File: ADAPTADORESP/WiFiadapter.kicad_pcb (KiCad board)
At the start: 2 copper layers, 30 x 31.2 mm, 9 parts, among them J1 ADAP_ESP, U1 ESP8266-12E/ESP-12E

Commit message: PCBS_Adap_mon
Correxión del RX y TX del adaptador, PCB monitor doble capa.
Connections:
- J1 pad 7: /TX -> /RX
- J1 pad 9: /RX -> /TX
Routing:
- net /TX: track 48.8 -> 40.1 mm, vias 0 -> 1
- net GND: track 20.3 -> 16.3 mm
- net (no net): track 0.00 -> 3.97 mm
- net /RX: track 41.5 -> 45.3 mm
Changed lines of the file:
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@@
   (general
     (links 26)
-    (no_connects 0)
+    (no_connects 1)
     (area 134.899999 96.274999 165.075001 127.575001)
     (thickness 1.6)
     (drawings 6)
-    (tracks 198)
+    (tracks 200)
     (zones 0)
     (modules 9)
@@
       (net 7 /D3))
     (pad 7 thru_hole oval (at 0 7.62 90) (size 1.7 1.7) (drill 1) (layers *.Cu *.Mask)
-      (net 14 /TX))
+      (net 12 /RX))
     (pad 8 thru_hole oval (at 2.54 7.62 90) (size 1.7 1.7) (drill 1) (layers *.Cu *.Mask)
       (net 5 /D2))
     (pad 9 thru_hole oval (at 0 10.16 90) (size 1.7 1.7) (drill 1) (layers *.Cu *.Mask)
-      (net 12 /RX))
+      (net 14 /TX))
     (pad 10 thru_hole oval (at 2.54 10.16 90) (size 1.7 1.7) (drill 1) (layers *.Cu *.Mask)
       (net 10 /SDA))
@@
     (arrow2b (pts (xy 135.0264 83.7184) (xy 136.152904 83.131979)))
   )
+  (segment (start 139 121.95) (end 139 120.5) (width 0.5) (layer F.Cu) (net 0))
+  (segment (start 139 120.5) (end 138.4 119.9) (width 0.5) (layer F.Cu) (net 0))
+  (segment (start 140.2 123.1) (end 140.15 123.1) (width 0.5) (layer B.Cu) (net 0))
+  (segment (start 140.15 123.1) (end 139 121.95) (width 0.5) (layer B.Cu) (net 0))
   (segment (start 160.2 112.55) (end 159.05 112.55) (width 0.5) (layer F.Cu) (net 1))
   (segment (start 159.05 112.55) (end 158.85 112.35) (width 0.5) (layer F.Cu) (net 1))
@@
   (segment (start 157.1625 111.8281) (end 158.6625 111.8281) (width 0.5) (layer F.Cu) (net 1))
   (segment (start 158.6625 111.8281) (end 158.85 112.0156) (width 0.5) (layer F.Cu) (net 1))
-  (segment (start 139 121.95) (end 139 120.5) (width 0.5) (layer F.Cu) (net 1))
-  (segment (start 139 120.5) (end 138.4 119.9) (width 0.5) (layer F.Cu) (net 1))
-  (segment (start 140.2 123.1) (end 140.15 123.1) (width 0.5) (layer B.Cu) (net 1))
-  (segment (start 140.15 123.1) (end 139 121.95) (width 0.5) (layer B.Cu) (net 1))
   (segment (start 143.02 123.14) (end 140.24 123.14) (width 0.5) (layer F.Cu) (net 1))
   (segment (start 140.24 123.14) (end 140.2 123.1) (width 0.5) (layer F.Cu) (net 1))
@@
   (via (at 159.15 107.8) (size 1) (drill 0.4) (layers F.Cu B.Cu) (net 11))
   (segment (start 153.95 115.85) (end 158.2 115.85) (width 0.3) (layer B.Cu) (net 11))
-  (segment (start 153.75 125.2) (end 153.18 124.63) (width 0.3) (layer F.Cu) (net 12))
-  (segment (start 153.18 124.63) (end 153.18 123.14) (width 0.3) (layer F.Cu) (net 12))
-  (segment (start 163.35 100.925) (end 163.35 122.95) (width 0.3) (layer F.Cu) (net 12))
-  (segment (start 163.35 122.95) (end 161.1 125.2) (width 0.3) (layer F.Cu) (net 12))
-  (segment (start 161.1 125.2) (end 153.75 125.2) (width 0.3) (layer F.Cu) (net 12))
-  (segment (start 157.1625 99.8281) (end 162.2531 99.8281) (width 0.3) (layer F.Cu) (net 12))
-  (segment (start 162.2531 99.8281) (end 163.35 100.925) (width 0.3) (layer F.Cu) (net 12))
+  (segment (start 150.64 123.14) (end 150.64 124.615) (width 0.3) (layer F.Cu) (net 12) (status 400000))
+  (segment (start 162.3781 99.8281) (end 157.1625 99.8281) (width 0.3) (layer F.Cu) (net 12) (status 800000))
+  (segment (start 163.725 101.175) (end 162.3781 99.8281) (width 0.3) (layer F.Cu) (net 12))
+  (segment (start 163.725 123.45) (end 163.725 101.175) (width 0.3) (layer F.Cu) (net 12))
+  (segment (start 161.525 125.65) (end 163.725 123.45) (width 0.3) (layer F.Cu) (net 12))
+  (segment (start 151.675 125.65) (end 161.525 125.65) (width 0.3) (layer F.Cu) (net 12))
+  (segment (start 150.64 124.615) (end 151.675 125.65) (width 0.3) (layer F.Cu) (net 12))
   (segment (start 160.65 117.75) (end 160.65 122.4) (width 0.3) (layer B.Cu) (net 13))
   (segment (start 160.65 117) (end 160.65 117.75) (width 0.3) (layer B.Cu) (net 13))
@@
   (segment (start 159.1719 105.8281) (end 159.2 105.8) (width 0.3) (layer F.Cu) (net 13))
   (via (at 159.2 105.8) (size 1) (drill 0.4) (layers F.Cu B.Cu) (net 13))
-  (segment (start 150.64 125.24) (end 150.64 123.14) (width 0.3) (layer F.Cu) (net 14))
-  (segment (start 151.8 126.4) (end 150.64 125.24) (width 0.3) (layer F.Cu) (net 14))
-  (segment (start 157.1625 97.8281) (end 162.6281 97.8281) (width 0.3) (layer F.Cu) (net 14))
-  (segment (start 162.6281 97.8281) (end 164 99.2) (width 0.3) (layer F.Cu) (net 14))
-  (segment (start 164 99.2) (end 164 123.4) (width 0.3) (layer F.Cu) (net 14))
-  (segment (start 164 123.4) (end 161 126.4) (width 0.3) (layer F.Cu) (net 14))
-  (segment (start 161 126.4) (end 151.8 126.4) (width 0.3) (layer F.Cu) (net 14))
+  (segment (start 160.85 97.925) (end 157.2594 97.925) (width 0.3) (layer F.Cu) (net 14))
+  (segment (start 157.2594 97.925) (end 157.1625 97.8281) (width 0.3) (layer F.Cu) (net 14))
+  (segment (start 161.875 122.9) (end 161.875 98.95) (width 0.3) (layer B.Cu) (net 14))
+  (segment (start 161.875 98.95) (end 160.85 97.925) (width 0.3) (layer B.Cu) (net 14))
+  (via (at 160.85 97.925) (size 1) (drill 0.4) (layers F.Cu B.Cu) (net 14))
+  (segment (start 159.875 124.9) (end 161.875 122.9) (width 0.3) (layer B.Cu) (net 14))
+  (segment (start 153.737919 124.9) (end 159.875 124.9) (width 0.3) (layer B.Cu) (net 14))
+  (segment (start 153.18 123.14) (end 153.18 124.342081) (width 0.3) (layer B.Cu) (net 14))
+  (segment (start 153.18 124.342081) (end 153.737919 124.9) (width 0.3) (layer B.Cu) (net 14))
   (segment (start 139.35 101.8) (end 142.1344 101.8) (width 0.5) (layer F.Cu) (net 21))
   (segment (start 142.1344 101.8) (end 142.1625 101.8281) (width 0.5) (layer F.Cu) (net 21))

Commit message: Adapter_TXRX
TX RX change
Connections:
- J1 pad 7: /RX -> /TX
- J1 pad 9: /TX -> /RX
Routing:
- net /TX: track 40.1 -> 47.0 mm, vias 1 -> 0
- net /RX: track 45.3 -> 40.2 mm
- net (no net): track 3.97 -> 0.05 mm
- net /D0: track 34.8 -> 35.7 mm
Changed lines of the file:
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@@
-(kicad_pcb (version 4) (host pcbnew 4.0.6)
+(kicad_pcb (version 4) (host pcbnew 4.0.7)
   (general
     (links 26)
-    (no_connects 0)
+    (no_connects 2)
     (area 134.899999 96.274999 165.075001 127.575001)
     (thickness 1.6)
     (drawings 6)
-    (tracks 200)
+    (tracks 201)
     (zones 0)
     (modules 9)
@@
       (net 7 /D3))
     (pad 7 thru_hole oval (at 0 7.62 90) (size 1.7 1.7) (drill 1) (layers *.Cu *.Mask)
-      (net 12 /RX))
+      (net 14 /TX))
     (pad 8 thru_hole oval (at 2.54 7.62 90) (size 1.7 1.7) (drill 1) (layers *.Cu *.Mask)
       (net 5 /D2))
     (pad 9 thru_hole oval (at 0 10.16 90) (size 1.7 1.7) (drill 1) (layers *.Cu *.Mask)
-      (net 14 /TX))
+      (net 12 /RX))
     (pad 10 thru_hole oval (at 2.54 10.16 90) (size 1.7 1.7) (drill 1) (layers *.Cu *.Mask)
       (net 10 /SDA))
@@
     (arrow2b (pts (xy 135.0264 83.7184) (xy 136.152904 83.131979)))
   )
-  (segment (start 139 121.95) (end 139 120.5) (width 0.5) (layer F.Cu) (net 0))
-  (segment (start 139 120.5) (end 138.4 119.9) (width 0.5) (layer F.Cu) (net 0))
   (segment (start 140.2 123.1) (end 140.15 123.1) (width 0.5) (layer B.Cu) (net 0))
-  (segment (start 140.15 123.1) (end 139 121.95) (width 0.5) (layer B.Cu) (net 0))
+  (segment (start 143.02 123.14) (end 140.24 123.14) (width 0.5) (layer F.Cu) (net 1))
   (segment (start 160.2 112.55) (end 159.05 112.55) (width 0.5) (layer F.Cu) (net 1))
   (segment (start 159.05 112.55) (end 158.85 112.35) (width 0.5) (layer F.Cu) (net 1))
@@
   (segment (start 157.1625 111.8281) (end 158.6625 111.8281) (width 0.5) (layer F.Cu) (net 1))
   (segment (start 158.6625 111.8281) (end 158.85 112.0156) (width 0.5) (layer F.Cu) (net 1))
-  (segment (start 143.02 123.14) (end 140.24 123.14) (width 0.5) (layer F.Cu) (net 1))
   (segment (start 140.24 123.14) (end 140.2 123.1) (width 0.5) (layer F.Cu) (net 1))
   (via (at 156.875 114.4) (size 1.2) (drill 0.6) (layers F.Cu B.Cu) (net 1))
@@
   (segment (start 139.9 107) (end 140.3 106.6) (width 0.3) (layer F.Cu) (net 3))
   (segment (start 140.3 106.6) (end 140.3 106.15) (width 0.3) (layer F.Cu) (net 3))
+  (segment (start 145.56 124.342081) (end 144.66 125.242081) (width 0.3) (layer F.Cu) (net 4))
+  (segment (start 140 125.375) (end 144.527081 125.375) (width 0.3) (layer F.Cu) (net 4))
+  (segment (start 144.527081 125.375) (end 144.66 125.242081) (width 0.3) (layer F.Cu) (net 4))
   (segment (start 137.075 122.5) (end 137.075 106.95) (width 0.3) (layer F.Cu) (net 4))
   (segment (start 137.075 106.95) (end 137.625 106.4) (width 0.3) (layer F.Cu) (net 4))
@@
   (segment (start 139.75 105.8) (end 139.75 104.5281) (width 0.3) (layer F.Cu) (net 4))
   (segment (start 140.45 103.8281) (end 142.1625 103.8281) (width 0.3) (layer F.Cu) (net 4))
-  (segment (start 141.7 125.4) (end 140.925 125.4) (width 0.3) (layer F.Cu) (net 4))
   (segment (start 140 125.375) (end 141.675 125.375) (width 0.3) (layer F.Cu) (net 4))
   (segment (start 145.56 123.14) (end 145.56 124.342081) (width 0.3) (layer F.Cu) (net 4))
-  (segment (start 144.502081 125.4) (end 141.7 125.4) (width 0.3) (layer F.Cu) (net 4))
   (segment (start 141.675 125.375) (end 141.7 125.4) (width 0.3) (layer F.Cu) (net 4))
-  (segment (start 145.56 124.342081) (end 144.502081 125.4) (width 0.3) (layer F.Cu) (net 4))
   (segment (start 140 125.375) (end 137.075 122.45) (width 0.3) (layer F.Cu) (net 4))
   (segment (start 150.64 120.6) (end 150.64 116.79) (width 0.3) (layer F.Cu) (net 5))
@@
   (via (at 159.15 107.8) (size 1) (drill 0.4) (layers F.Cu B.Cu) (net 11))
   (segment (start 153.95 115.85) (end 158.2 115.85) (width 0.3) (layer B.Cu) (net 11))
-  (segment (start 150.64 123.14) (end 150.64 124.615) (width 0.3) (layer F.Cu) (net 12))
-  (segment (start 162.3781 99.8281) (end 157.1625 99.8281) (width 0.3) (layer F.Cu) (net 12))
-  (segment (start 163.725 101.175) (end 162.3781 99.8281) (width 0.3) (layer F.Cu) (net 12))
-  (segment (start 163.725 123.45) (end 163.725 101.175) (width 0.3) (layer F.Cu) (net 12))
-  (segment (start 161.525 125.65) (end 163.725 123.45) (width 0.3) (layer F.Cu) (net 12))
-  (segment (start 151.675 125.65) (end 161.525 125.65) (width 0.3) (layer F.Cu) (net 12))
-  (segment (start 150.64 124.615) (end 151.675 125.65) (width 0.3) (layer F.Cu) (net 12))
+  (segment (start 153.18 123.14) (end 153.18 124.45) (width 0.3) (layer F.Cu) (net 12))
+  (segment (start 153.18 124.45) (end 153.48 124.75) (width 0.3) (layer F.Cu) (net 12))
+  (segment (start 158.4625 99.8281) (end 157.1625 99.8281) (width 0.3) (layer F.Cu) (net 12))
+  (segment (start 153.48 124.75) (end 159.64 124.75) (width 0.3) (layer F.Cu) (net 12))
+  (segment (start 159.64 124.75) (end 163.54 120.85) (width 0.3) (layer F.Cu) (net 12))
+  (segment (start 163.54 120.85) (end 163.54 100.91) (width 0.3) (layer F.Cu) (net 12))
+  (segment (start 163.54 100.91) (end 162.46 99.83) (width 0.3) (layer F.Cu) (net 12))
+  (segment (start 162.46 99.83) (end 158.4644 99.83) (width 0.3) (layer F.Cu) (net 12))
+  (segment (start 158.4644 99.83) (end 158.4625 99.8281) (width 0.3) (layer F.Cu) (net 12))
   (segment (start 160.65 117.75) (end 160.65 122.4) (width 0.3) (layer B.Cu) (net 13))
   (segment (start 160.65 117) (end 160.65 117.75) (width 0.3) (layer B.Cu) (net 13))
@@
   (segment (start 159.1719 105.8281) (end 159.2 105.8) (width 0.3) (layer F.Cu) (net 13))
   (via (at 159.2 105.8) (size 1) (drill 0.4) (layers F.Cu B.Cu) (net 13))
-  (segment (start 160.85 97.925) (end 157.2594 97.925) (width 0.3) (layer F.Cu) (net 14))
+  (segment (start 150.63 124.6) (end 150.64 124.59) (width 0.3) (layer F.Cu) (net 14))
+  (segment (start 150.64 124.59) (end 150.64 123.14) (width 0.3) (layer F.Cu) (net 14))
+  (segment (start 151.460008 125.430008) (end 150.63 124.6) (width 0.3) (layer F.Cu) (net 14))
+  (segment (start 164.38 121.2) (end 160.149992 125.430008) (width 0.3) (layer F.Cu) (net 14))
+  (segment (start 160.149992 125.430008) (end 151.460008 125.430008) (width 0.3) (layer F.Cu) (net 14))
+  (segment (start 164.38 99.72) (end 164.38 121.2) (width 0.3) (layer F.Cu) (net 14))
+  (segment (start 162.585 97.925) (end 164.38 99.72) (width 0.3) (layer F.Cu) (net 14))
+  (segment (start 160.67 97.925) (end 157.2594 97.925) (width 0.3) (layer F.Cu) (net 14))
+  (segment (start 160.85 97.925) (end 160.67 97.925) (width 0.3) (layer F.Cu) (net 14))
+  (segment (start 160.67 97.925) (end 162.585 97.925) (width 0.3) (layer F.Cu) (net 14))
   (segment (start 157.2594 97.925) (end 157.1625 97.8281) (width 0.3) (layer F.Cu) (net 14))
-  (segment (start 161.875 122.9) (end 161.875 98.95) (width 0.3) (layer B.Cu) (net 14))
-  (segment (start 161.875 98.95) (end 160.85 97.925) (width 0.3) (layer B.Cu) (net 14))
-  (via (at 160.85 97.925) (size 1) (drill 0.4) (layers F.Cu B.Cu) (net 14))
-  (segment (start 159.875 124.9) (end 161.875 122.9) (width 0.3) (layer B.Cu) (net 14))
-  (segment (start 153.737919 124.9) (end 159.875 124.9) (width 0.3) (layer B.Cu) (net 14))
-  (segment (start 153.18 123.14) (end 153.18 124.342081) (width 0.3) (layer B.Cu) (net 14))
-  (segment (start 153.18 124.342081) (end 153.737919 124.9) (width 0.3) (layer B.Cu) (net 14))
   (segment (start 139.35 101.8) (end 142.1344 101.8) (width 0.5) (layer F.Cu) (net 21))
   (segment (start 142.1344 101.8) (end 142.1625 101.8281) (width 0.5) (layer F.Cu) (net 21))

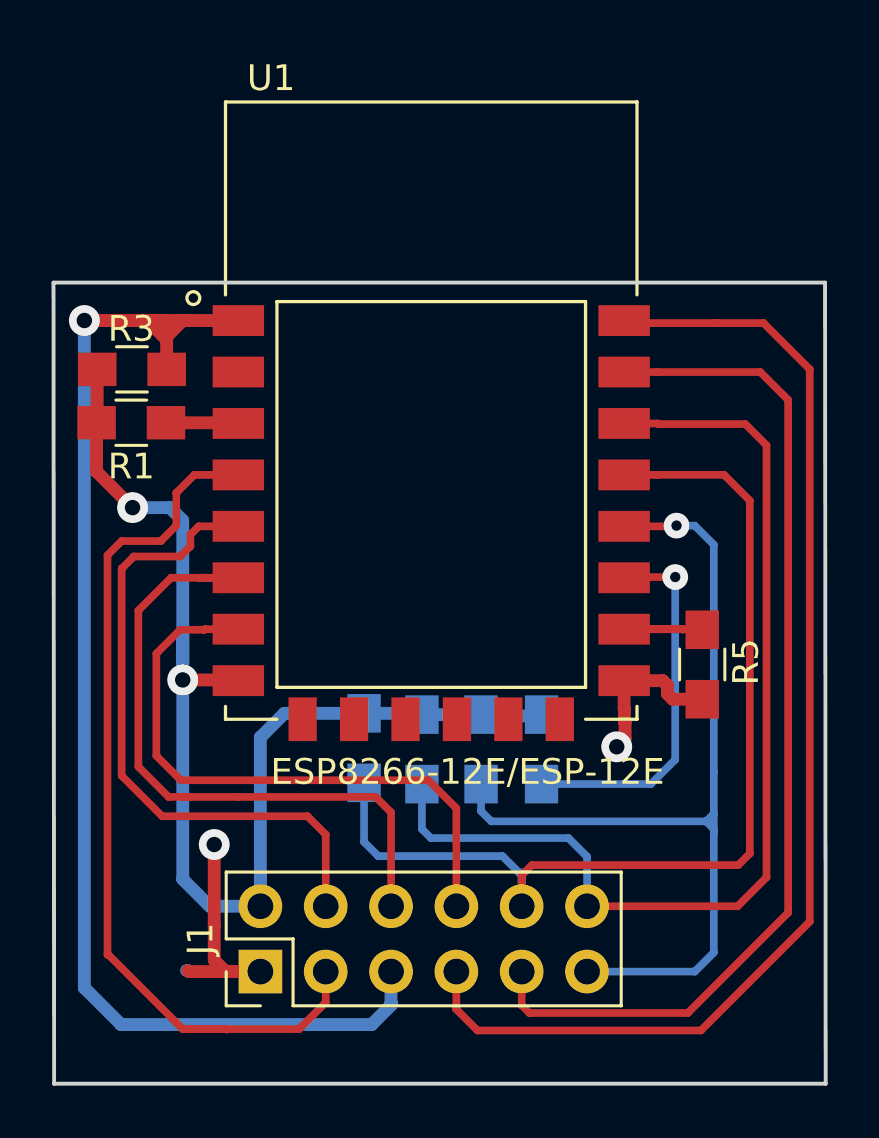
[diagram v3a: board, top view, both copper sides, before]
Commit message: pcb_adapter
Redondeo de la placa
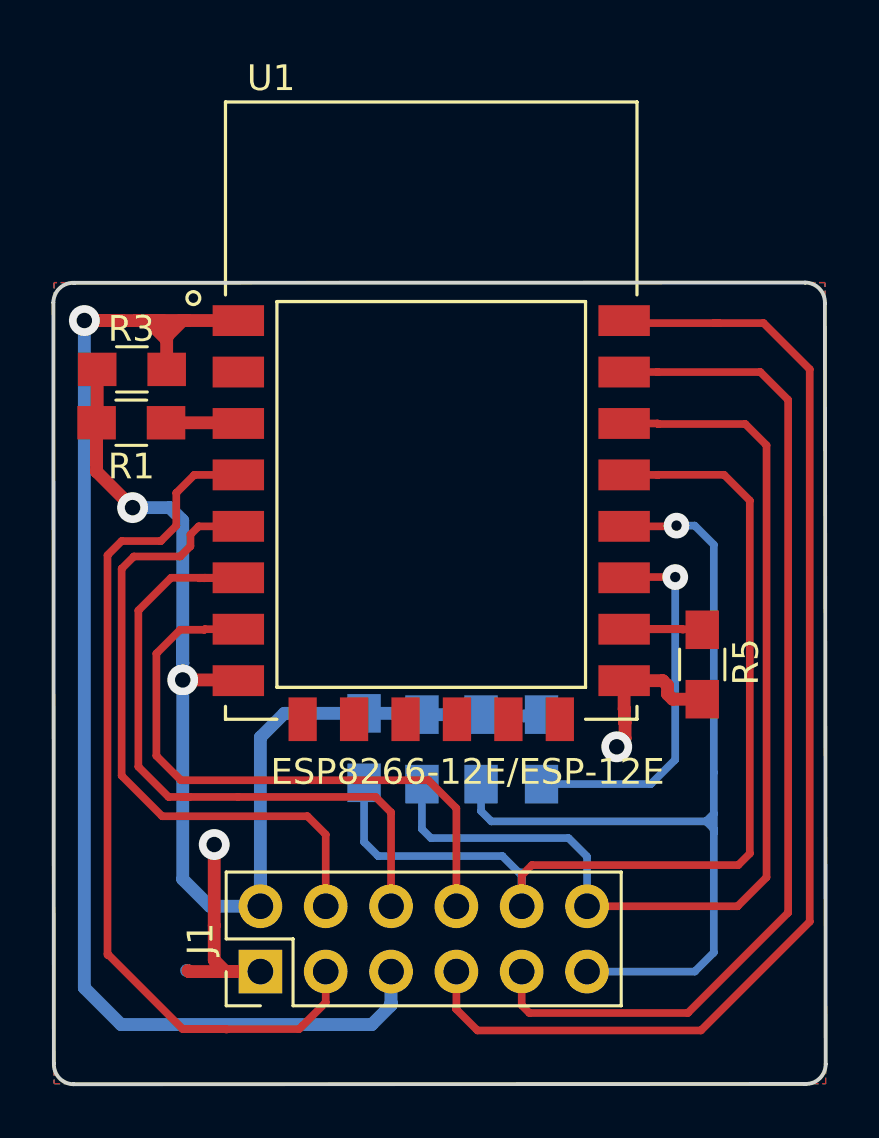
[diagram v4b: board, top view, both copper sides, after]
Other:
- outline, holes or cut-outs redrawn
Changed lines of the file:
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@@
   (general
     (links 26)
-    (no_connects 2)
-    (area 134.899999 96.274999 165.075001 127.575001)
+    (no_connects 0)
+    (area 134.896062 96.274999 165.075001 127.595001)
     (thickness 1.6)
-    (drawings 6)
+    (drawings 10)
     (tracks 201)
     (zones 0)
@@
     )
   )
-  (gr_line (start 164.975 96.35) (end 165 127.5) (angle 90) (layer Edge.Cuts) (width 0.15))
-  (gr_line (start 135 127.5) (end 134.975 96.35) (angle 90) (layer Edge.Cuts) (width 0.15))
-  (gr_line (start 165 127.5) (end 135 127.5) (angle 90) (layer Edge.Cuts) (width 0.15))
-  (gr_line (start 134.975 96.35) (end 164.975 96.35) (angle 90) (layer Edge.Cuts) (width 0.15))
+  (gr_arc (start 135.76 126.75) (end 135.76 127.52) (angle 92.89854576) (layer Edge.Cuts) (width 0.15))
+  (gr_arc (start 135.741063 97.129015) (end 134.971063 97.129015) (angle 92.89854576) (layer Edge.Cuts) (width 0.15))
+  (gr_arc (start 164.2 97.12) (end 164.2 96.35) (angle 92.89854576) (layer Edge.Cuts) (width 0.15))
+  (gr_arc (start 164.23 126.74) (end 165 126.74) (angle 92.89854576) (layer Edge.Cuts) (width 0.15))
+  (gr_line (start 164.97 97.16) (end 165 126.74) (angle 90) (layer Edge.Cuts) (width 0.15))
+  (gr_line (start 134.99 126.71) (end 134.97 97.13) (angle 90) (layer Edge.Cuts) (width 0.15))
+  (gr_line (start 164.19 127.51) (end 135.76 127.52) (angle 90) (layer Edge.Cuts) (width 0.15))
+  (gr_line (start 135.77 96.36) (end 164.2 96.35) (angle 90) (layer Edge.Cuts) (width 0.15))
   (dimension 40.259 (width 0.3) (layer Margin)
     (gr_text "40.259 mm" (at 176.4576 107.5055 270) (layer Margin)

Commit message: Change GPIO16 to GPIO09
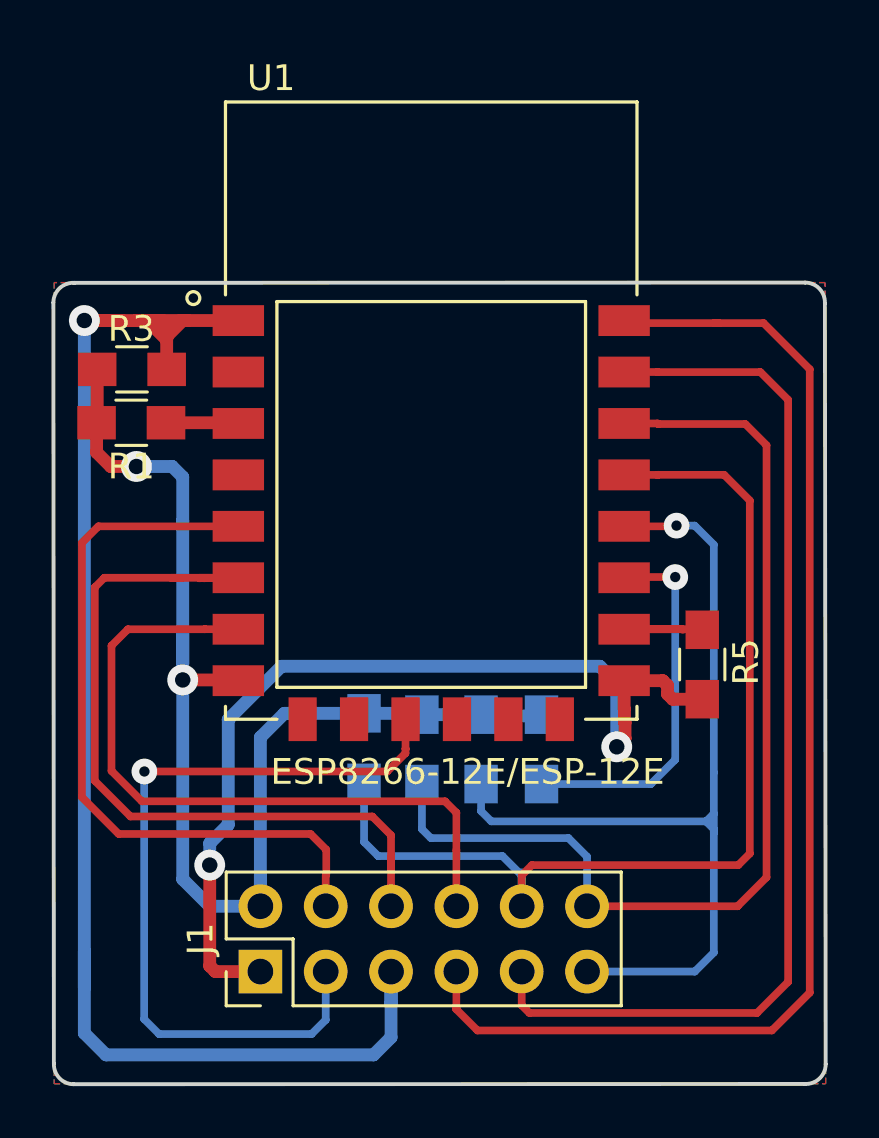
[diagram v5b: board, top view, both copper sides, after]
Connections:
- U1 pad 11: Net-(U1-Pad11) -> /D0
- U1 pad 4: /D0 -> Net-(U1-Pad4)
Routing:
- net GND: track 16.3 -> 36.9 mm
- net /RST: track 52.8 -> 58.2 mm
- net /D0: track 35.7 -> 30.8 mm, vias 0 -> 1
- net /D3: track 26.5 -> 30.9 mm
- net /D2: track 23.9 -> 27.8 mm
- net /D1: track 25.2 -> 28.8 mm
- net /TX: track 47.0 -> 48.6 mm
- net /RX: track 40.2 -> 41.8 mm
- net +3V3: track 49.7 -> 49.0 mm
